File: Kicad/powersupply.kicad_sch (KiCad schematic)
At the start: 26 parts, among them J1101 Jack 2.1{slash}6.3mm, J1102 Conn_02x02S, J1103 Conn_01x04S, Q1101 AO3401A, Q1102 SS8550, Q1103 SS8050, U1101 DC-DC Module, U1102 AMS1117-3.3, U1103 LP2950N

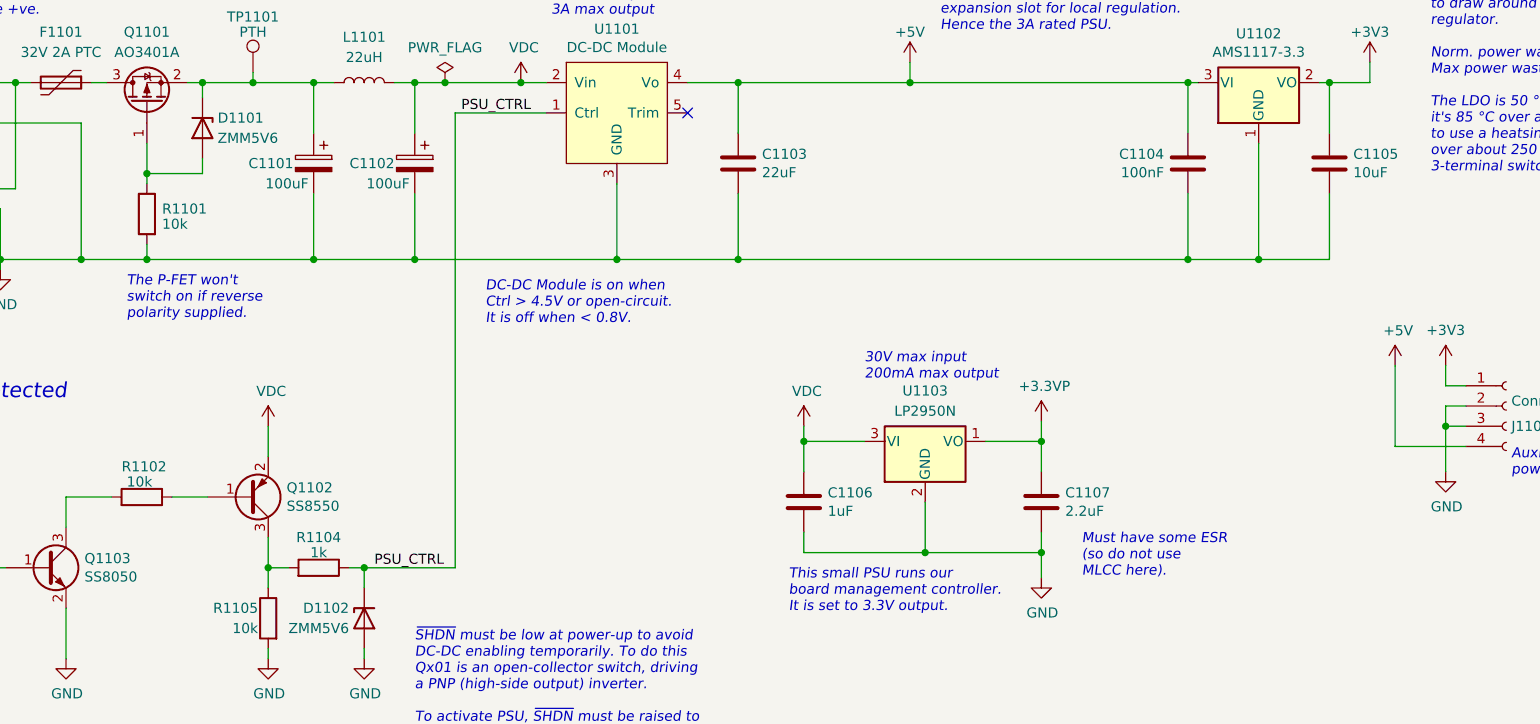
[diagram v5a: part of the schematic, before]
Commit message: Replaced decoupling caps, and worked on PCB layout.
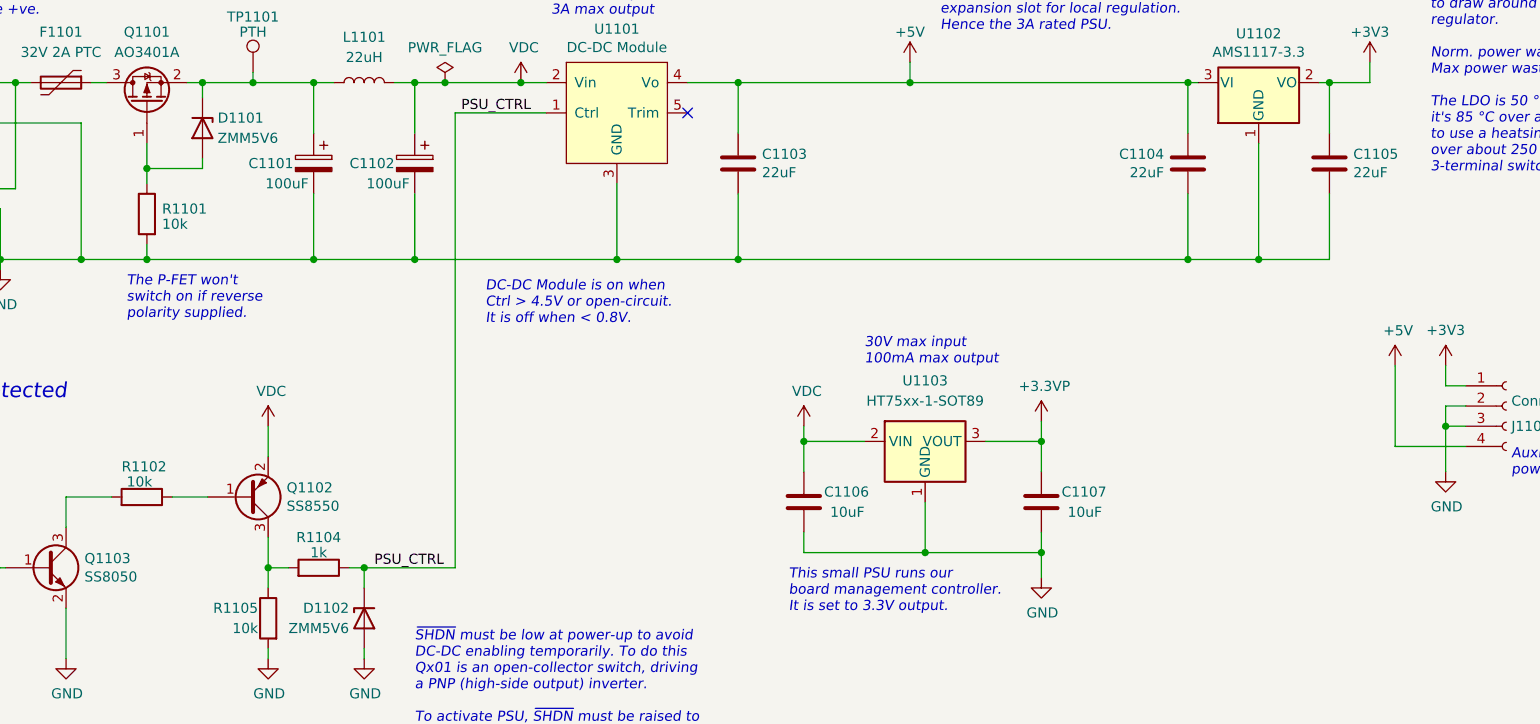
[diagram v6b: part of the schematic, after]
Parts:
- removed U1103: LP2950N, Package_TO_SOT_THT:TO-92_Inline, symbol Regulator_Linear:LP2950-3.3_TO92
- added U1103: HT75xx-1-SOT89, Package_TO_SOT_SMD:SOT-89-3, symbol Regulator_Linear:HT75xx-1-SOT89
- C1104: value 100nF -> 22uF; JLCPCB Collection Basic -> Extended; LCSC Part# C49678 -> C602037; MPN CC0805KRX7R9BB104 -> CL21A226MAYNNNE; Manufacturer Yageo -> Samsung; Tolerance X7R -> X5R; Voltage 50V -> 25V
- C1105: value 10uF -> 22uF; JLCPCB Collection Basic -> Extended; LCSC Part# C15850 -> C602037; MPN CL21A106KAYNNNE -> CL21A226MAYNNNE
- C1106: value 1uF -> 10uF; LCSC Part# C28323 -> C15850; MPN CL21B105KBFNNNE -> CL21A106KAYNNNE; Tolerance X7R -> X5R; Voltage 50V -> 25V
- C1107: value 2.2uF -> 10uF; footprint Capacitor_SMD:CP_Elec_4x5.4 -> Capacitor_SMD:C_0805_2012Metric_Pad1.18x1.45mm_HandSolder; JLCPCB Collection Extended -> Basic; LCSC Part# C72492 -> C15850; MPN RVT1C2R2M0405 -> CL21A106KAYNNNE; Manufacturer Roqang -> Samsung; Tolerance 20% -> X5R; Voltage 16V -> 25V
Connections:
- net +3.3VP: now also C1107.2, U1103.3 (VOUT); no longer C1107.1
- net GND: now also C1106.1, C1107.1, U1103.1 (GND); no longer C1106.2, C1107.2
- net VDC: now also C1106.2, U1103.2 (VIN); no longer C1106.1
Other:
- note added: "30V max input 100mA max output"
- note removed: "30V max input 200mA max output"
- note removed: "Must have some ESR (so do not use MLCC here)."

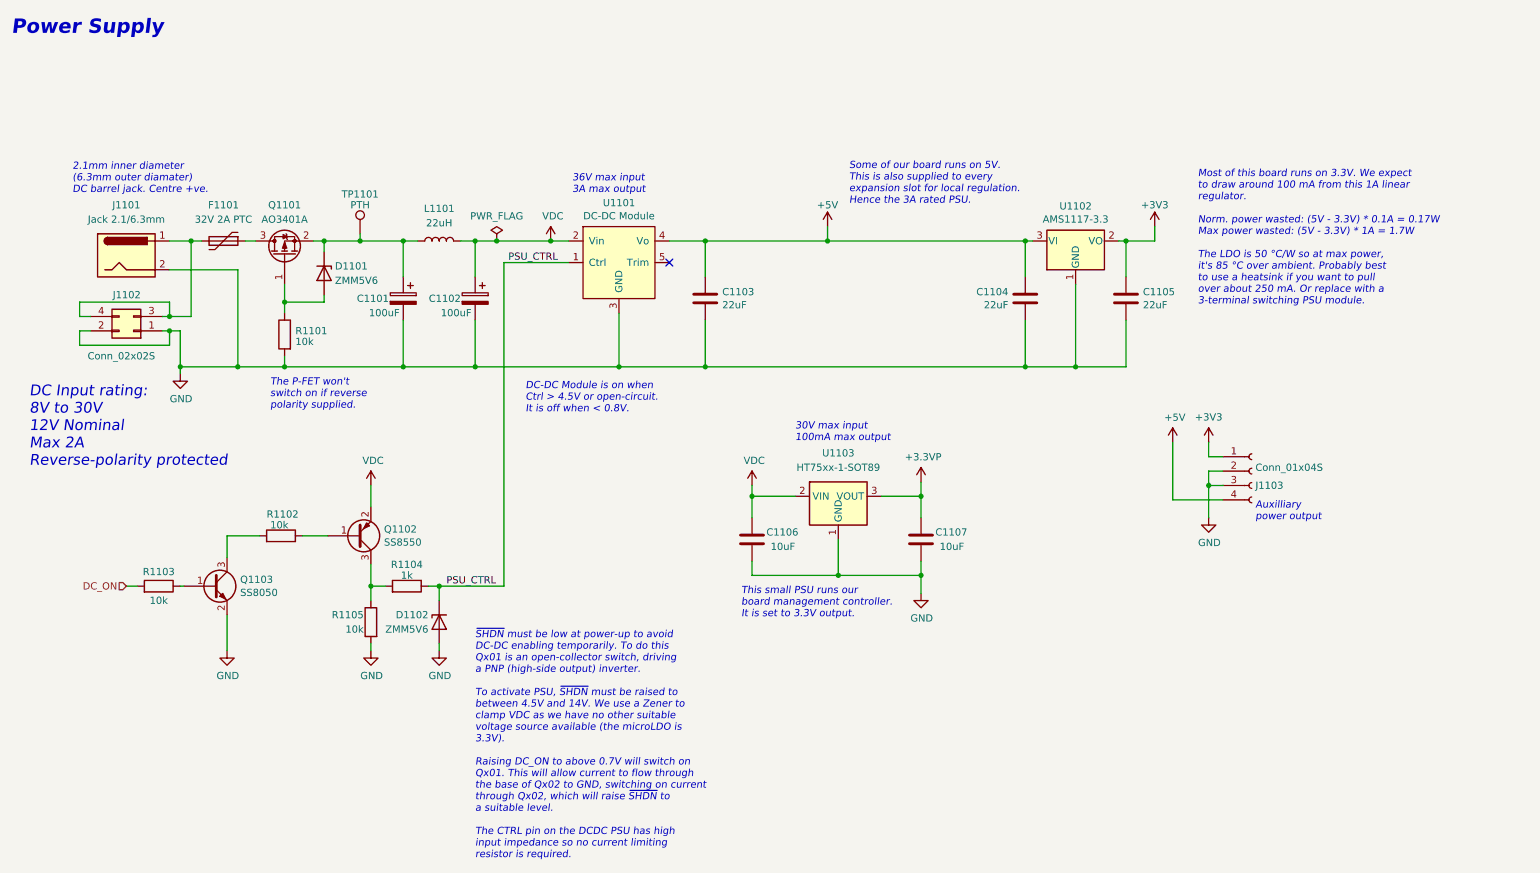
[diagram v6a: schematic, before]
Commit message: Added source resistors on SPI bus.
Also renumbered pages.
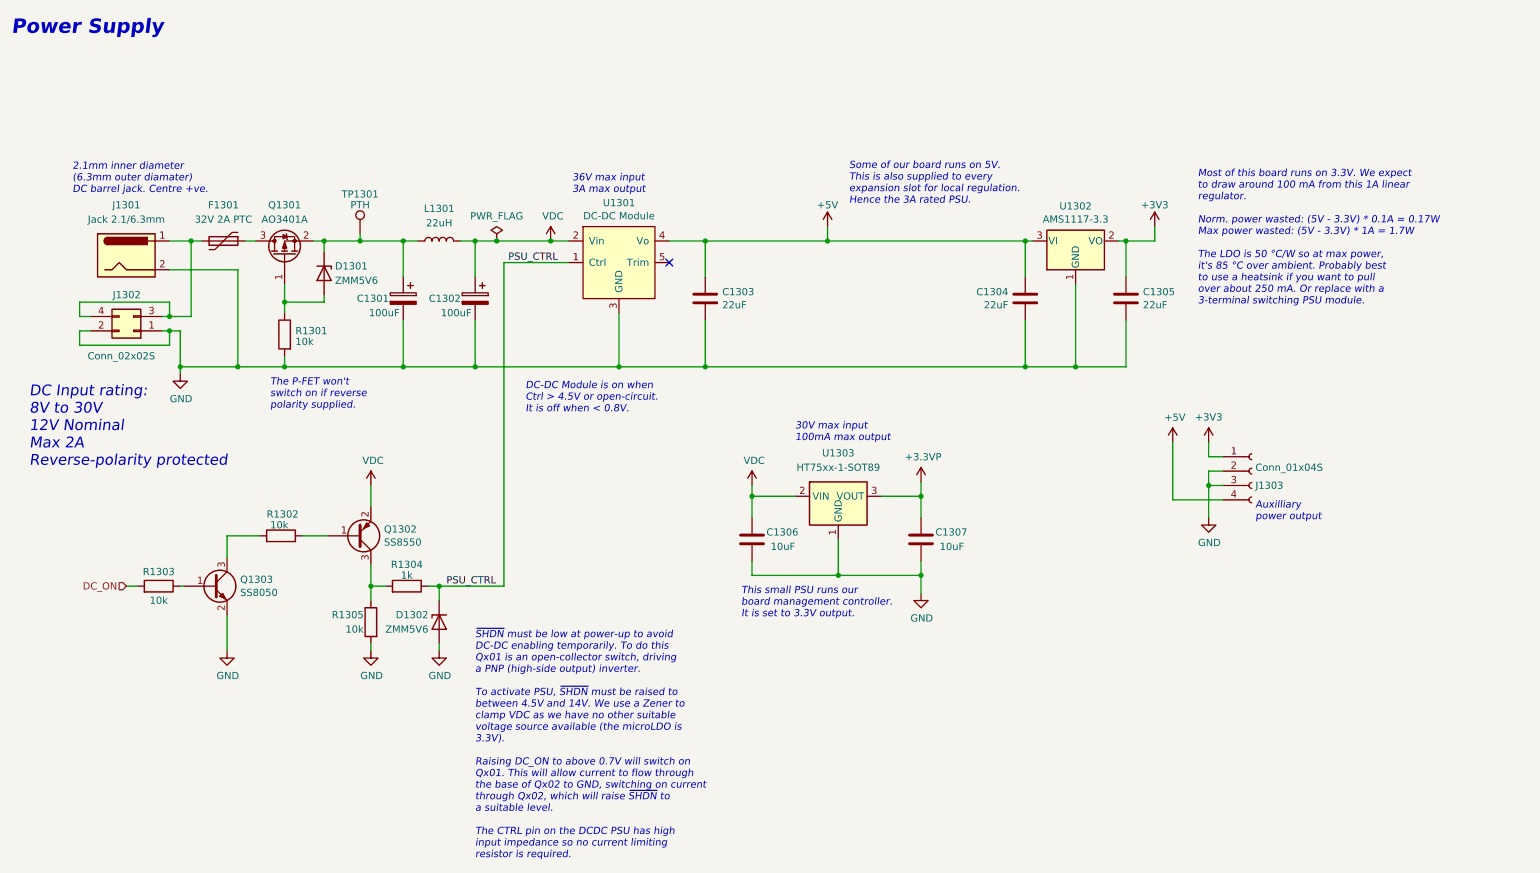
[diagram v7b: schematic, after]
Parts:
- renumbered C1101 to C1301, C1102 to C1302, C1103 to C1303, C1104 to C1304, C1105 to C1305, C1106 to C1306, C1107 to C1307, D1101 to D1301, D1102 to D1302, F1101 to F1301, J1101 to J1301, J1102 to J1302, J1103 to J1303, L1101 to L1301, Q1101 to Q1301, Q1102 to Q1302, Q1103 to Q1303, R1101 to R1301, R1102 to R1302, R1103 to R1303, R1104 to R1304, R1105 to R1305, TP1101 to TP1301, U1101 to U1301, U1102 to U1302, U1103 to U1303

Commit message: Fix micro LDO metadata.
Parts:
- U1303: DNP (none) -> 0; JLCPCB Collection (none) -> Basic; LCSC Part# (none) -> C14289; MPN (none) -> HT7533-1; Manufacturer (none) -> Holtek
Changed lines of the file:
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@@
+      (effects (font (size 1.27 1.27)) hide)
+    )
+    (property "DNP" "0" (id 5) (at 158.75 101.6 0)
+      (effects (font (size 1.27 1.27)) hide)
+    )
+    (property "Digikey" "~" (id 6) (at 158.75 101.6 0)
+      (effects (font (size 1.27 1.27)) hide)
+    )
+    (property "JLCPCB Collection" "Basic" (id 7) (at 158.75 101.6 0)
+      (effects (font (size 1.27 1.27)) hide)
+    )
+    (property "LCSC Part#" "C14289" (id 8) (at 158.75 101.6 0)
+      (effects (font (size 1.27 1.27)) hide)
+    )
+    (property "MPN" "HT7533-1" (id 9) (at 158.75 101.6 0)
+      (effects (font (size 1.27 1.27)) hide)
+    )
+    (property "Manufacturer" "Holtek" (id 10) (at 158.75 101.6 0)
+      (effects (font (size 1.27 1.27)) hide)
+    )
+    (property "Mouser" "~" (id 11) (at 158.75 101.6 0)
+      (effects (font (size 1.27 1.27)) hide)
+    )
+    (property "Tolerance" "~" (id 12) (at 158.75 101.6 0)
+      (effects (font (size 1.27 1.27)) hide)
+    )
+    (property "Voltage" "~" (id 13) (at 158.75 101.6 0)
       (effects (font (size 1.27 1.27)) hide)
     )
